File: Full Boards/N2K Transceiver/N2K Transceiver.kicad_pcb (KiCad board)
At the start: 4 copper layers, 80 x 60 mm, 76 parts, among them J1 Optional Bond, J3 JTAG, SW1 SW_MEC_5G, SW2 SW_MEC_5G, SW3 SW_MEC_5G

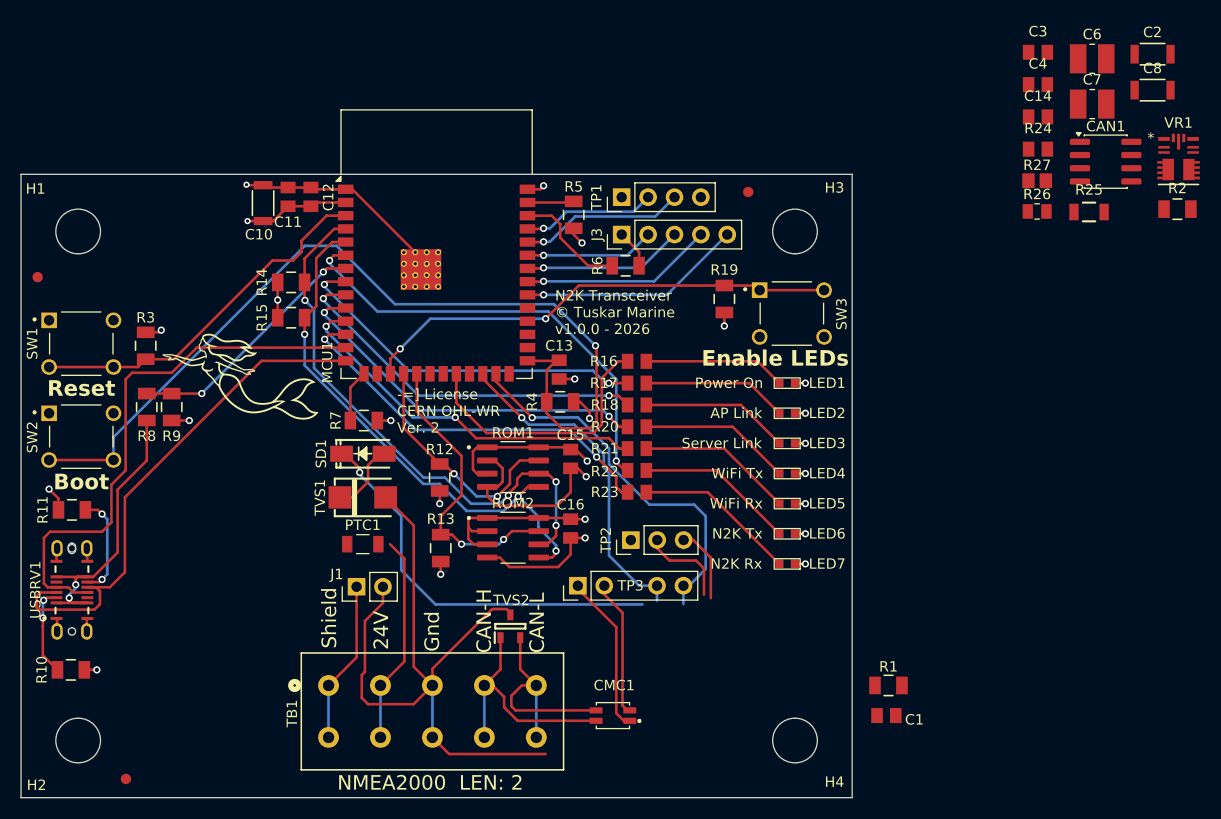
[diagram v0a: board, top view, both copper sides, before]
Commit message: Reworked PCB for new non-isolated design, one odd DRC error remains though.
Signed-off-by: digimer <digital.mermaid@gmail.com>
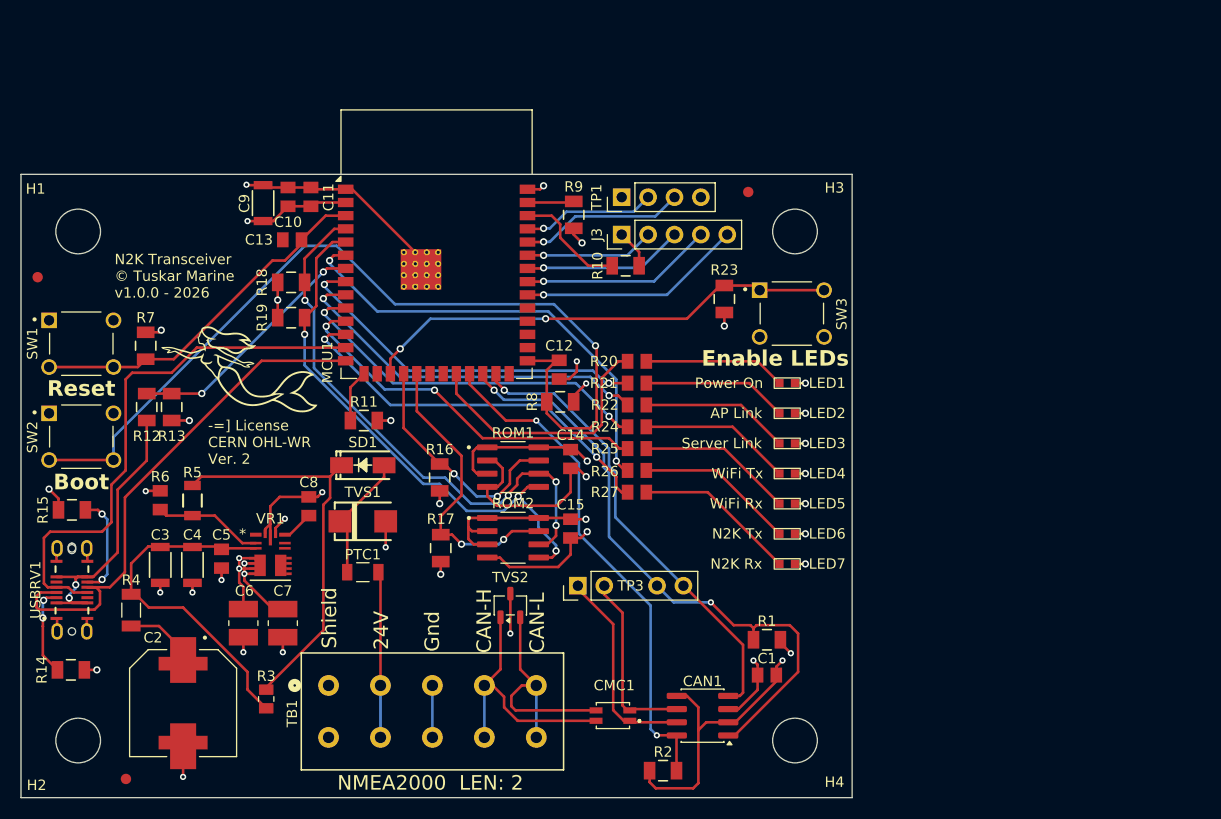
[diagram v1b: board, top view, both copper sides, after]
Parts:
- removed J1: Optional Bond, Connector_PinHeader_2.54mm:PinHeader_1x02_P2.54mm_Vertical
- removed the R26 at (157.8, 46.9)
- removed the R27 at (157.8, 43.9)
- removed TP2: Ship Power, Connector_PinHeader_2.54mm:PinHeader_1x03_P2.54mm_Vertical
- added C2: 330uF, mr-stuff:Panasonic EEH-ZU, F.Cu at (75.6, 94.2)
- added R3: 0R, mr-stuff:Vishay RCA-SR e3, F.Cu at (83.6, 93.8)
- added R4: 0.2R, mr-stuff:KOA SR73, F.Cu at (70.6, 85.2)
- TVS2: value PESD2CANFD54VT-QR -> VCAN33A2-03SHE3A08; footprint mr-stuff:Nexperia PESD2CANFD -> mr-stuff:Vishay VCAN33A2-03S
- moved C3 105.9 mm to (73.4, 80.9), turned to -90 degrees
- moved C4 104.7 mm to (76.5, 80.9), turned to -90 degrees
- moved C6 98.1 mm to (81.4, 86.5), turned to -90 degrees
- moved VR1 95.4 mm to (84.0, 80.0)
- moved C7 92.6 mm to (85.2, 86.5), turned to -90 degrees
- moved C5 92.5 mm to (79.3, 80.3), turned to -90 degrees
- moved R6 91.0 mm to (73.4, 74.7), turned to 90 degrees
- moved R5 90.7 mm to (76.5, 74.7), turned to 90 degrees
- moved C8 81.1 mm to (87.7, 75.2), turned to 90 degrees
- moved R2 73.3 mm to (121.8, 100.7)
- moved C13 72.8 mm to (86.1, 49.6), turned to 180 degrees
- moved CAN1 65.9 mm to (125.6, 95.4), turned to 180 degrees
- moved R1 12.5 mm to (131.8, 88.1), turned to 0 degrees
- moved C1 12.1 mm to (131.8, 91.5), turned to 180 degrees
- moved PTC1 2.70 mm to (92.9, 81.6)
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- renumbered C11 to C10, C12 to C11, C13 to C12, C14 to C13, C15 to C14, C16 to C15, C8 to C3, C2 to C4, C3 to C5, C4 to C8, C10 to C9, R6 to R10, R7 to R11, R8 to R12, R9 to R13, R10 to R14, R11 to R15, R12 to R16, R13 to R17, R14 to R18, R15 to R19, R16 to R20, R17 to R21, R18 to R22, R19 to R23, R20 to R24, R21 to R25, R22 to R26, R23 to R27, R25 to R5, R24 to R6, R3 to R7, R4 to R8, R5 to R9
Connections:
- C13 pad 1: /MCU_RESET -> Net-(MCU1-EN)
- MCU1 pad 20: /MCU_RESET -> unconnected-(MCU1-IO12-Pad20)
- MCU1 pad 3: /MCU_RESET -> Net-(MCU1-EN)
- R7 pad 1: /MCU_RESET -> Net-(MCU1-EN)
- SW1 pad 3: /MCU_RESET -> Net-(MCU1-EN)
- SW1 pad 4: /MCU_RESET -> Net-(MCU1-EN)
- TB1 pad 1: Net-(J1-Pin_1) -> unconnected-(TB1-Pad1)
- TB1 pad 2: Net-(J1-Pin_1) -> unconnected-(TB1-Pad2)
- TB1 pad 5: GND_SHIP -> GND
- TB1 pad 6: GND_SHIP -> GND
- TVS1 pad 2: GND_SHIP -> GND
- TVS2 pad 3: GND_SHIP -> GND
- VR1 pad 1: Net-(VR1-PGOOD) -> unconnected-(VR1-PGOOD-Pad1)
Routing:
- net GND_SHIP: track 76.3 -> 0.00 mm
- net GND: track 79.0 -> 136.4 mm, vias 17 -> 28
- net /CAN_STANDBY: track 0.00 -> 49.2 mm, vias 0 -> 2
- net /MCU_RESET: track 35.2 -> 0.00 mm
- net Net-(MCU1-EN): track 0.00 -> 34.4 mm
- net Net-(VR1-VIN): track 0.00 -> 33.5 mm
- net /CAN_TX_LOCAL: track 32.3 -> 58.6 mm, vias 1 -> 2
- net +3.3V: track 53.7 -> 78.1 mm, vias 9 -> 16
- net Net-(J1-Pin_1): track 15.6 -> 0.00 mm
- net Net-(VR1-EN): track 0.00 -> 10.5 mm
- net /CAN_RX_LOCAL: track 36.9 -> 44.7 mm
- net V_RAW: track 45.4 -> 38.0 mm, vias 1 -> 0
- net Net-(C2-Pad1): track 0.00 -> 5.96 mm
- net Net-(SD1-A): track 6.93 -> 11.4 mm
- net Net-(PTC1-Pad2): track 20.1 -> 15.7 mm
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
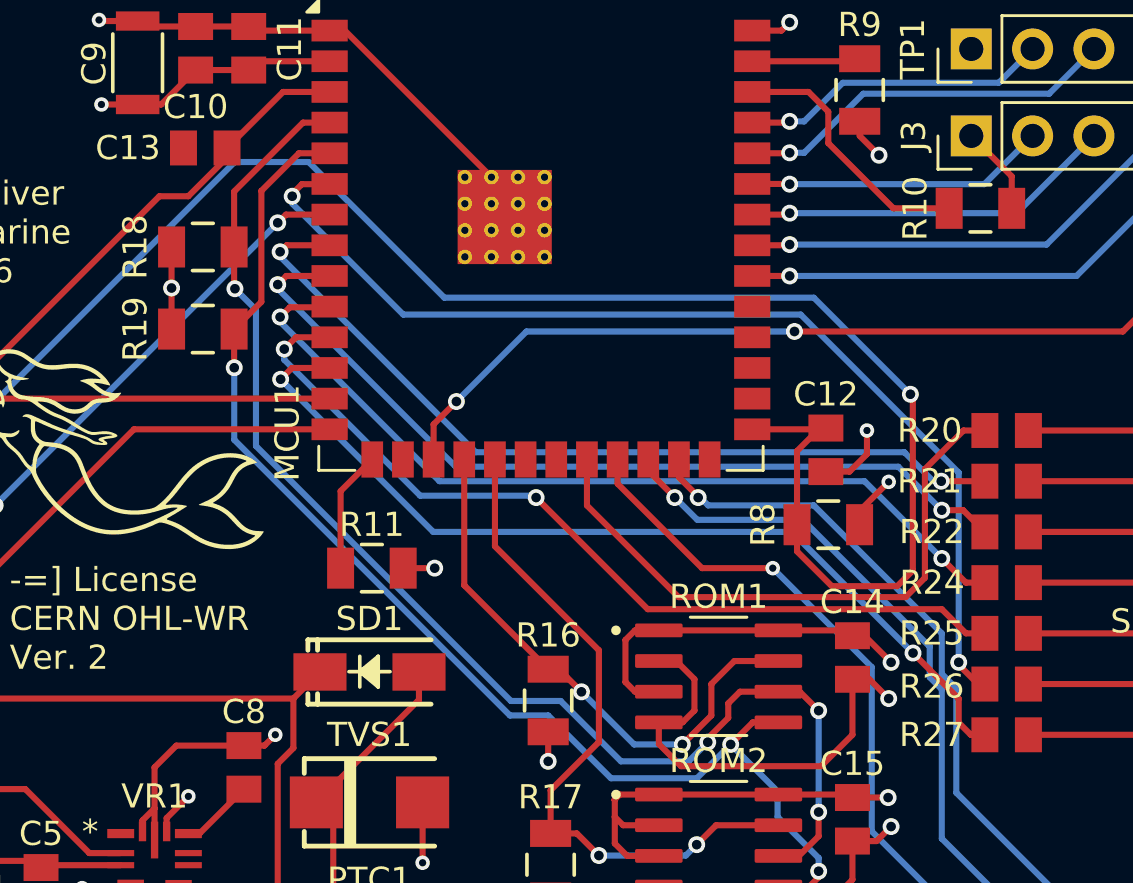
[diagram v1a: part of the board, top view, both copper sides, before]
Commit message: DRC issue resolved.
Signed-off-by: digimer <digital.mermaid@gmail.com>
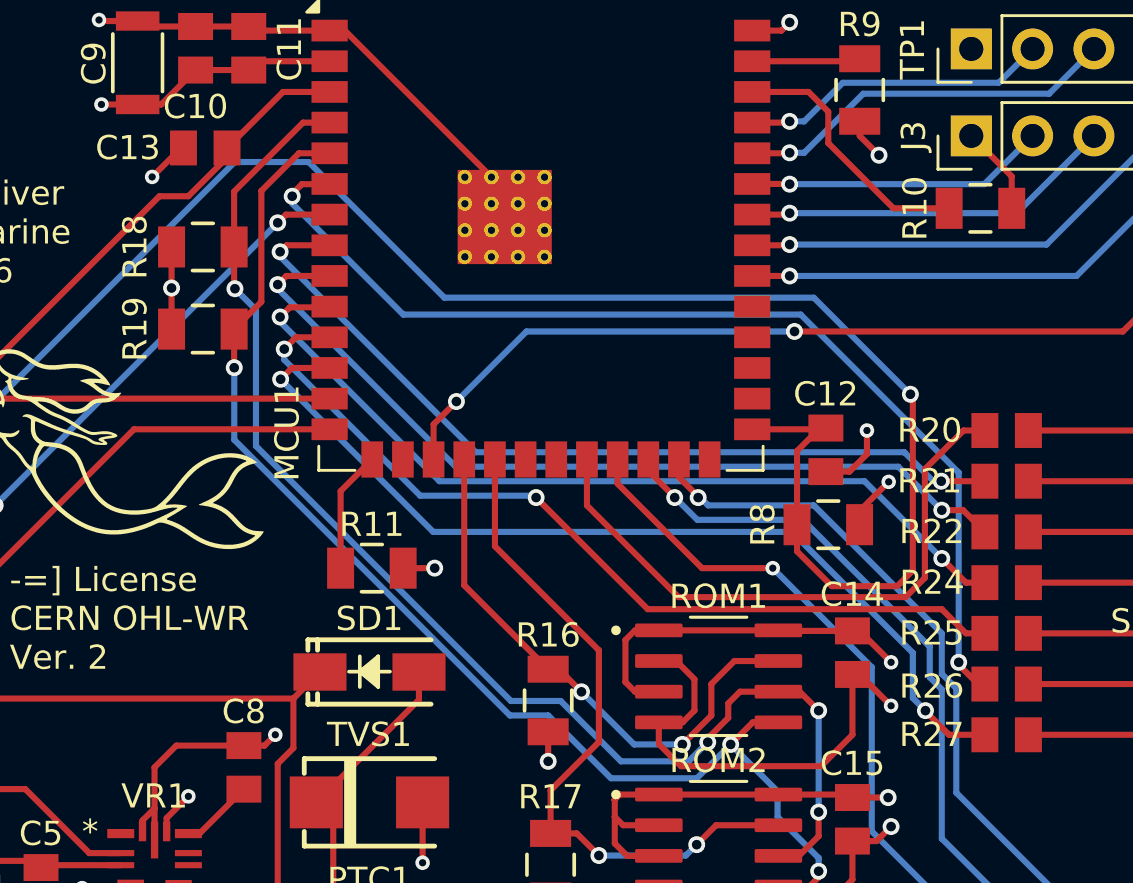
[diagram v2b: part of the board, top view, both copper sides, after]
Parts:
- moved C14 0.20 mm to (112.9, 70.5)
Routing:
- net GND: track 136.4 -> 138.3 mm, vias 28 -> 29
- net /N2K_RX_LED: track 38.1 -> 38.6 mm

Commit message: More cleanup
Signed-off-by: digimer <digital.mermaid@gmail.com>
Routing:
- net Net-(C2-Pad1): track 5.96 -> 7.26 mm
- net +3.3V: track 78.6 -> 79.5 mm
- net Net-(MCU1-IO1): track 3.74 -> 4.49 mm
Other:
- board text added: "NMEA2000 LEN: 1"
- board text removed: "NMEA2000 LEN: 2"
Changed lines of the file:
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@@
 		(tags "RNCP1206FTD3K01 ")
 		(property "Reference" "R12"
-			(at -2.8 0 0)
+			(at 2.7 0 0)
 			(unlocked yes)
 			(layer "F.SilkS")
@@
 		)
 	)
-	(gr_text "NMEA2000  LEN: 2"
+	(gr_text "NMEA2000  LEN: 1"
 		(at 99.4 102.7 0)
 		(layer "F.SilkS")
@@
 	)
 	(segment
+		(start 81.5 81.75)
+		(end 81.5 82.4)
+		(width 0.254)
+		(layer "F.Cu")
+		(net "+3.3V")
+	)
+	(segment
 		(start 113.1983 69.5983)
 		(end 114.5 70.9)
@@
 	)
 	(segment
-		(start 81.5 81.75)
-		(end 81.5 82.4)
+		(start 81 81.25)
+		(end 81 82.6)
 		(width 0.254)
 		(layer "F.Cu")
@@
 	)
 	(segment
-		(start 81 81.25)
-		(end 81 82.6)
+		(start 84.247 85.147)
+		(end 85.2 85.147)
 		(width 0.254)
 		(layer "F.Cu")
@@
 	)
 	(segment
+		(start 81.5 82.4)
+		(end 84.247 85.147)
+		(width 0.254)
+		(layer "F.Cu")
+		(net "+3.3V")
+	)
+	(segment
 		(start 114.3 76.5)
 		(end 114.2983 76.4983)
@@
 	)
 	(segment
-		(start 81.5 82.4)
-		(end 84.247 85.147)
-		(width 0.254)
-		(layer "F.Cu")
-		(net "+3.3V")
-	)
-	(segment
 		(start 84.5 77.35)
 		(end 85.4 76.45)
@@
 	)
 	(segment
+		(start 75.6 89.1)
+		(end 75.6 90.4)
+		(width 0.254)
+		(layer "F.Cu")
+		(net "Net-(C2-Pad1)")
+	)
+	(segment
 		(start 70.6 86.778)
 		(end 73.278 86.778)
@@
 	)
 	(segment
+		(start 113.0946 46.01)
+		(end 113.2 45.9046)
+		(width 0.254)
+		(layer "F.Cu")
+		(net "Net-(MCU1-IO1)")
+	)
+	(segment
 		(start 108.75 46.01)
-		(end 112.4946 46.01)
+		(end 113.0946 46.01)
 		(width 0.254)
 		(layer "F.Cu")

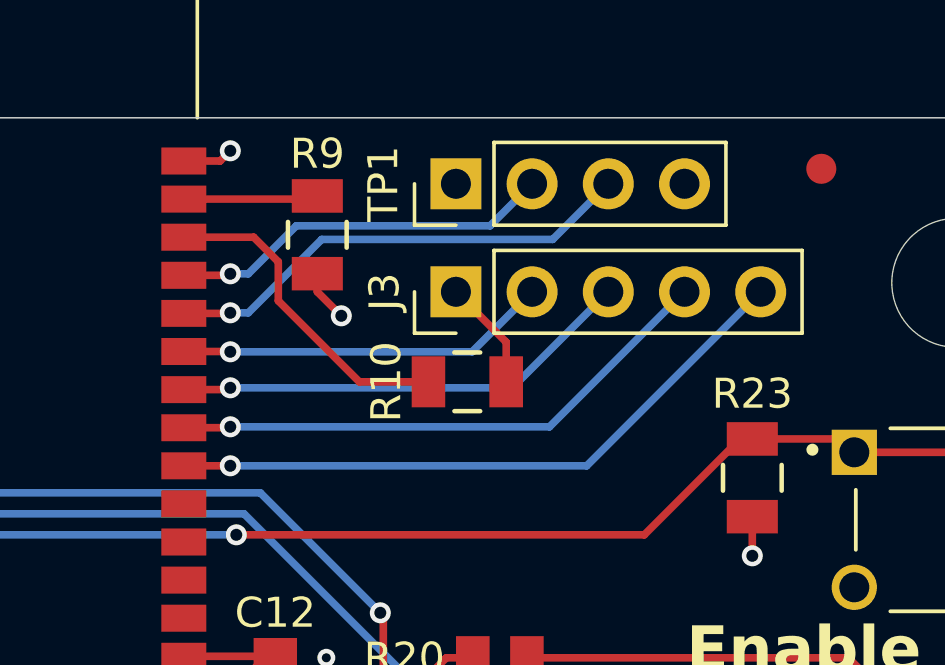
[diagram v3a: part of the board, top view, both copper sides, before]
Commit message: Cleaned up a few vias.
Signed-off-by: digimer <digital.mermaid@gmail.com>
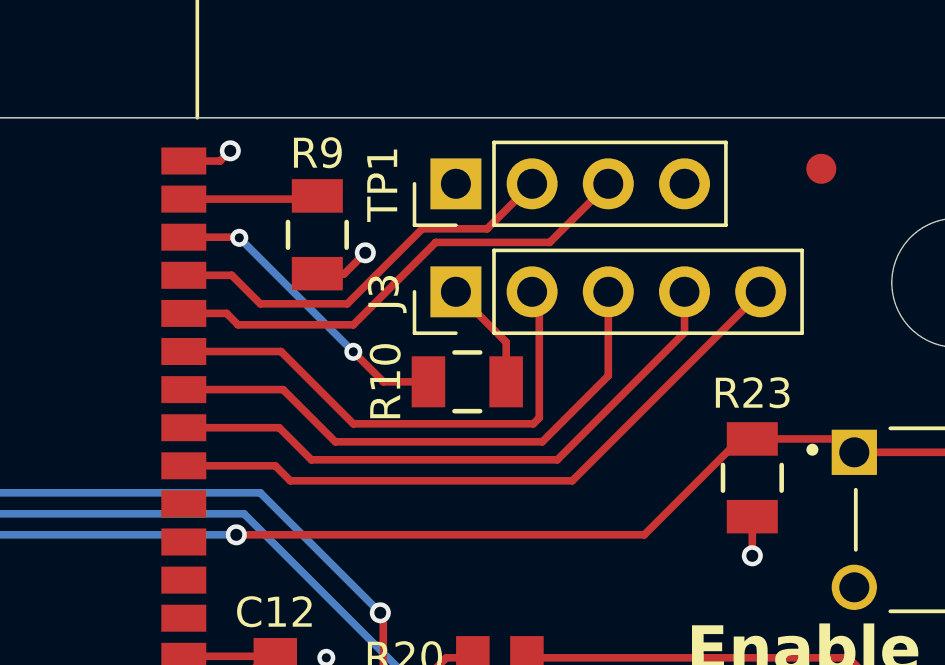
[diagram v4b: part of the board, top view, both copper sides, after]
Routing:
- net Net-(J3-Pin_2): track 12.4 -> 17.2 mm, vias 1 -> 0
- net Net-(J3-Pin_3): track 15.5 -> 18.6 mm, vias 1 -> 0
- net Net-(J3-Pin_4): track 18.6 -> 20.2 mm, vias 1 -> 0
- net Net-(MCU1-TXD0): track 12.9 -> 13.7 mm, vias 1 -> 0
- net Net-(MCU1-IO2): track 10.9 -> 10.2 mm, vias 0 -> 2
- net Net-(J3-Pin_5): track 21.6 -> 22.1 mm, vias 1 -> 0
- net Net-(MCU1-RXD0): track 15.9 -> 16.3 mm, vias 1 -> 0
